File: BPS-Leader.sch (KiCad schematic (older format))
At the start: 25 parts, among them J1 GPIO Analyzer, J2 Volt/Temp SPI Analyzer, J3 Current SPI Analyzer, J4 CAN Analyzer, J5 SWD, SW1 B3SL-1002P, U1 STM32F413RHTx, Y1 8M

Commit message: Adds HX1188 component to common library
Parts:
- U1: P/N (none) -> 7A-8.000MAHJ-T
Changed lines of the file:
@@
 F 2 "Package_QFP:LQFP-64_10x10mm_P0.5mm" H 5200 2200 50  0001 R CNN
 F 3 "http://www.st.com/st-web-ui/static/active/en/resource/technical/document/datasheet/DM00282249.pdf" H 5800 3900 50  0001 C CNN
+F 4 "" H 5800 3900 50  0001 C CNN "Field4"
+F 5 "7A-8.000MAHJ-T" H 5800 3900 50  0001 C CNN "P/N"
 	1    5800 3900
 	1    0    0    -1

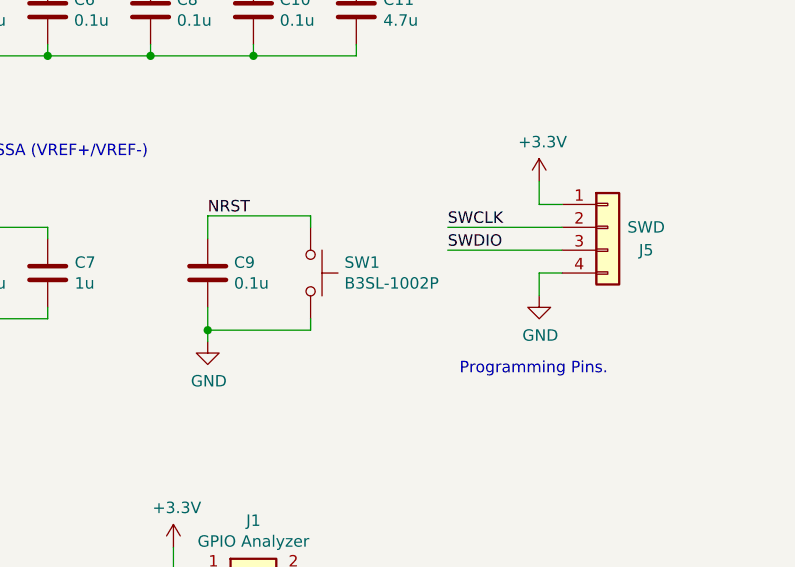
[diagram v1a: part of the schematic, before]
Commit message: Renames Reset button
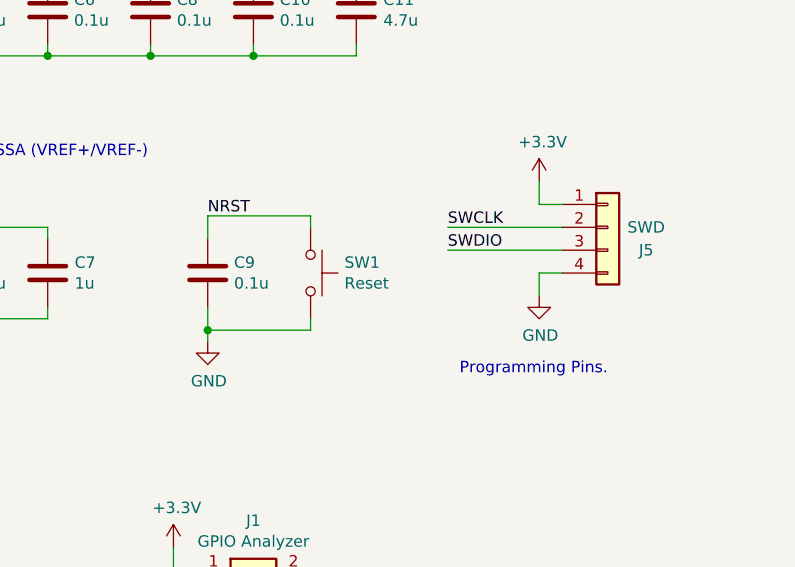
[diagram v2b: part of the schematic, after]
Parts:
- SW1: value B3SL-1002P -> Reset; P/N (none) -> B3SL-1002P
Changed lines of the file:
@@
 P 9550 2900
 F 0 "SW1" V 9504 3048 50  0000 L CNN
-F 1 "B3SL-1002P" V 9595 3048 50  0000 L CNN
+F 1 "Reset" V 9595 3048 50  0000 L CNN
 F 2 "Button_Switch_SMD:SW_SPST_B3SL-1002P" H 9550 3100 50  0001 C CNN
 F 3 "" H 9550 3100 50  0001 C CNN
+F 4 "B3SL-1002P" V 9550 2900 50  0001 C CNN "P/N"
 	1    9550 2900
 	0    1    1    0
